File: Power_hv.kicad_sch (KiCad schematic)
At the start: 19 parts, among them J4 Conn_Coaxial, U25 LT3080xDD

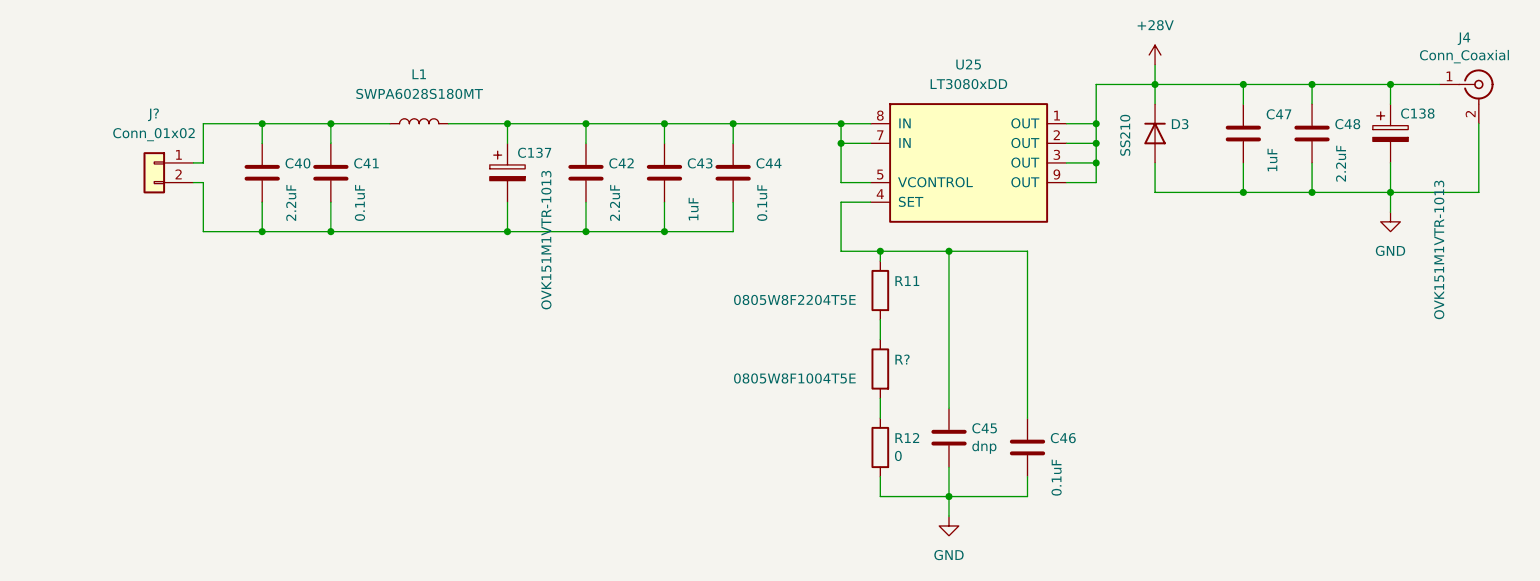
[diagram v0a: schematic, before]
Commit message: Preliminary layout of analog portions
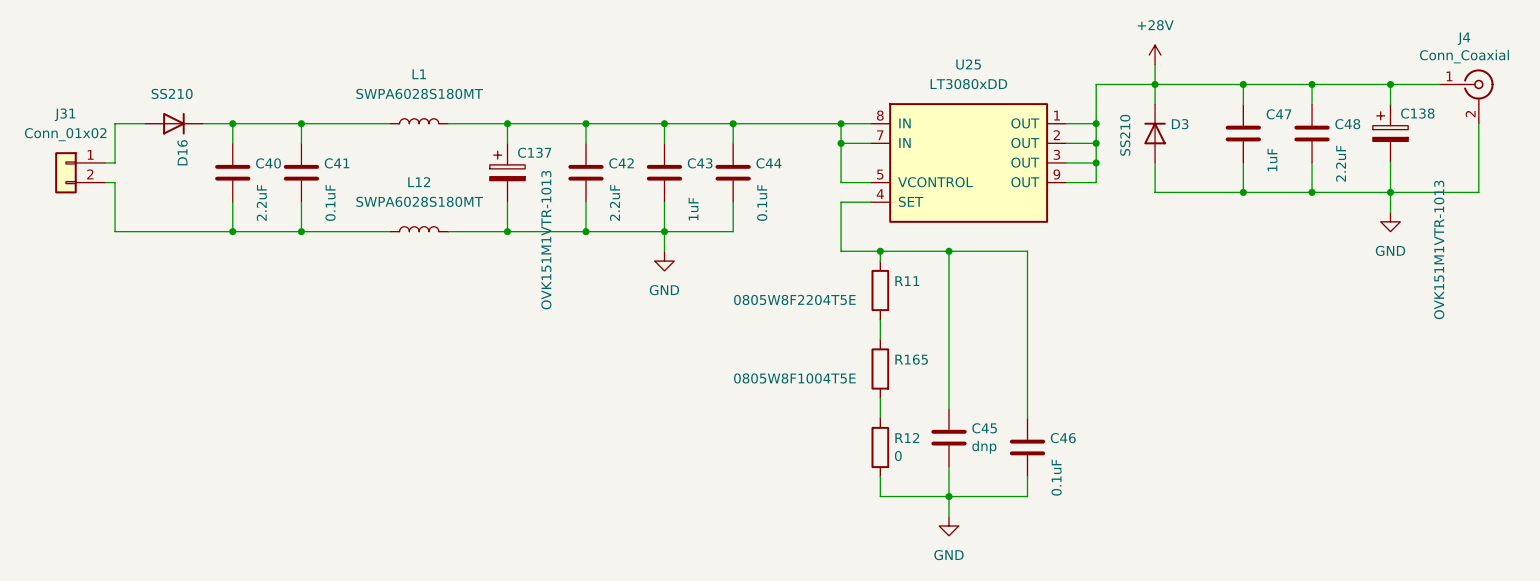
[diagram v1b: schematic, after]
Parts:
- added D16: SS210, Diode_SMD:D_SMA, symbol Device:D
- added L12: SWPA6028S180MT, Inductor_SMD:L_Bourns-SRN6028, symbol Device:L
- gave numbers to parts that had none: 2
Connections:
- net GND: now also C137.2, C42.2, C43.2, C44.2, L12.2
- net at C40.1, C41.1, L1.1: now also D16.1 (K); no longer J31.1 (Pin_1)
- new net: C40.2, C41.2, J31.2 (Pin_2), L12.1
- new net: D16.2 (A), J31.1 (Pin_1)
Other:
- moved on the sheet: C40, C41, J31

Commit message: First finished draft
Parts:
- C137, C138: symbol Device:CP -> Device:C_Polarized
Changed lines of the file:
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@@
     (pin "2")
   )
-  (symbol (lib_id "Device:CP") (at 205.74 83.82 0) (unit 1)
+  (symbol (lib_id "Device:C_Polarized") (at 205.74 83.82 0) (unit 1)
     (in_bom yes) (on_board yes)
     (property "Reference" "C138" (id 0) (at 207.01 81.28 0)
@@
     (pin "2")
   )
-  (symbol (lib_id "Device:CP") (at 91.44 88.9 0) (unit 1)
+  (symbol (lib_id "Device:C_Polarized") (at 91.44 88.9 0) (unit 1)
     (in_bom yes) (on_board yes)
     (property "Reference" "C137" (id 0) (at 92.71 86.36 0)

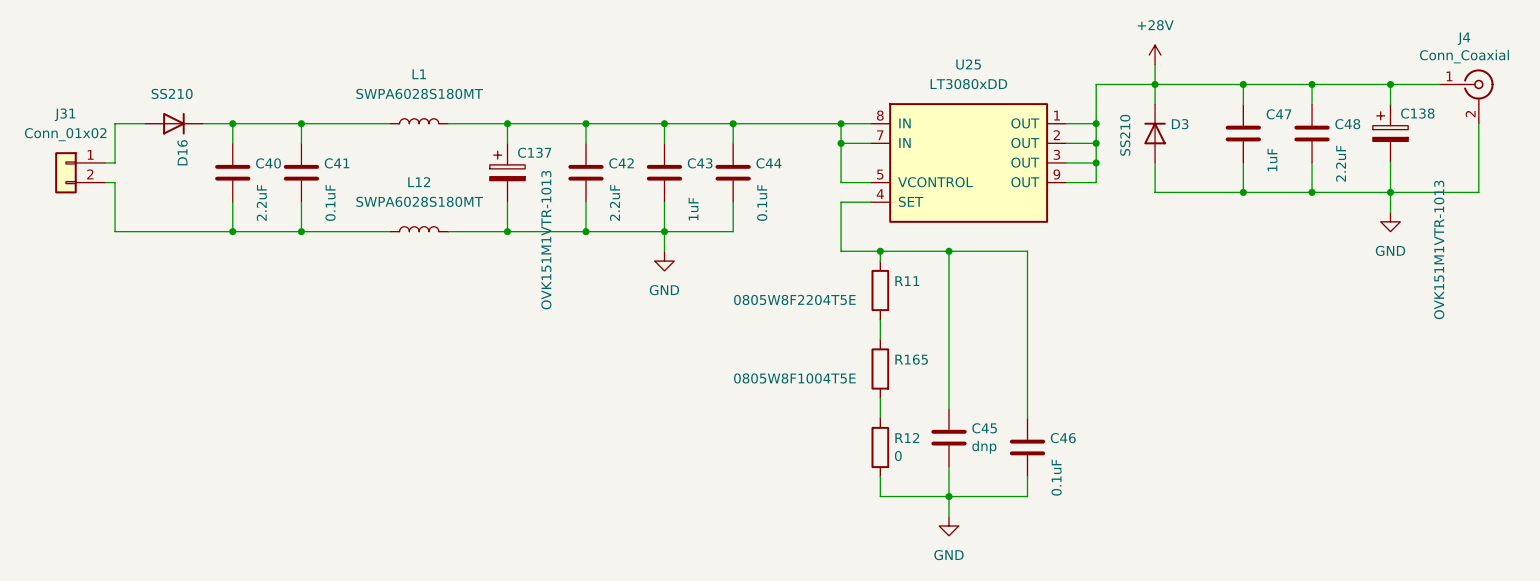
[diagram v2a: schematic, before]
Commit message: Version 1.0 submitted to JLCPCB
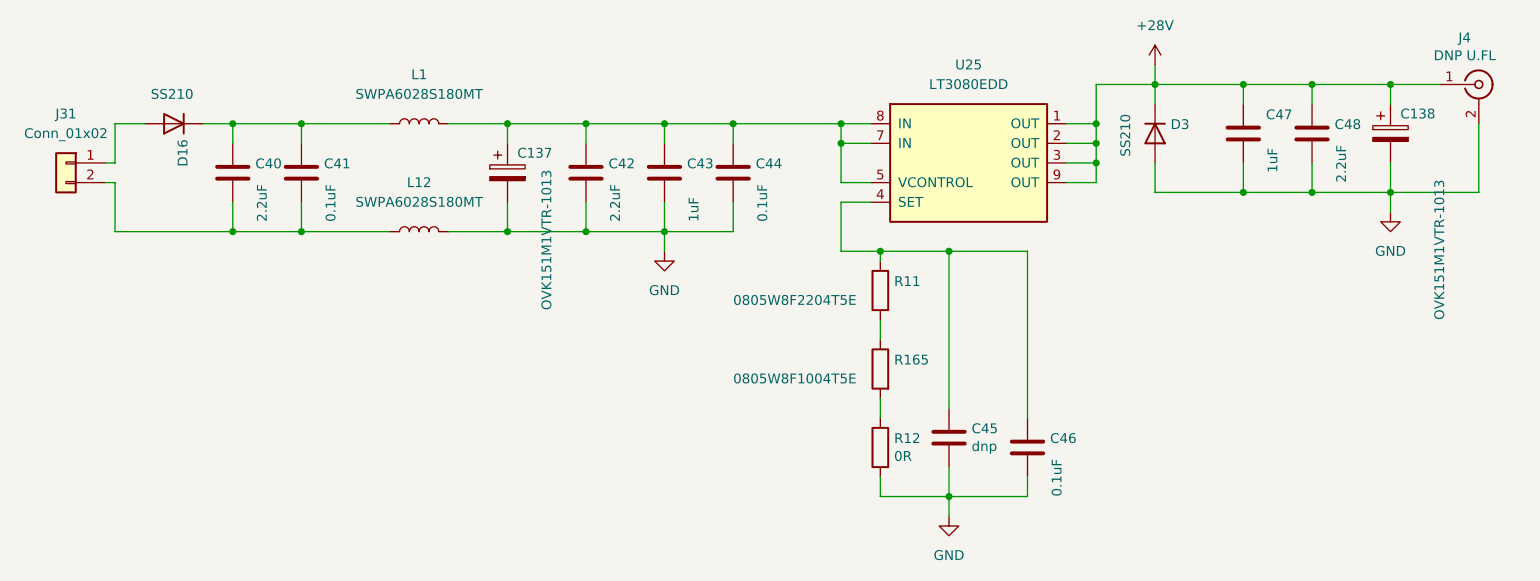
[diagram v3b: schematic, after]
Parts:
- J4: value Conn_Coaxial -> DNP U.FL
- R12: value 0 -> 0R
- U25: value LT3080xDD -> LT3080EDD
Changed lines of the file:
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@@
       (effects (font (size 1.27 1.27)) (justify right))
     )
-    (property "Value" "0" (id 1) (at 141.478 125.603 0)
+    (property "Value" "0R" (id 1) (at 141.478 125.603 0)
       (effects (font (size 1.27 1.27)) (justify right))
     )
@@
     (in_bom yes) (on_board yes) (fields_autoplaced)
     (property "Reference" "U25" (id 0) (at 151.13 74.93 0))
-    (property "Value" "LT3080xDD" (id 1) (at 151.13 77.47 0))
+    (property "Value" "LT3080EDD" (id 1) (at 151.13 77.47 0))
     (property "Footprint" "Package_DFN_QFN:DFN-8-1EP_3x3mm_P0.5mm_EP1.66x2.38mm" (id 2) (at 151.13 97.79 0)
       (effects (font (size 1.27 1.27)) hide)
@@
     (in_bom yes) (on_board yes)
     (property "Reference" "J4" (id 0) (at 215.3412 71.4248 0))
-    (property "Value" "Conn_Coaxial" (id 1) (at 215.3412 73.7362 0))
+    (property "Value" "DNP U.FL" (id 1) (at 215.3412 73.7362 0))
     (property "Footprint" "Connector_Coaxial:U.FL_Hirose_U.FL-R-SMT-1_Vertical" (id 2) (at 217.17 77.47 0)
       (effects (font (size 1.27 1.27)) hide)
